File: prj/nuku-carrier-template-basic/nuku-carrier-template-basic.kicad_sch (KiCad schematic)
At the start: 0 parts

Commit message: Route template.basic
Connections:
- no-connect marks 0 -> 2
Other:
- added sheet config (config.kicad_sch)
- added sheet pmod (pmod.kicad_sch)
- sheet bridge ports: added PWREN, SUSPEND, USB_DN, USB_DP, {JTAG}, {UART}; removed none
- sheet core-north-14 ports: added CLK, {CONFIG}; removed none
- sheet usb ports: added USB_DN, USB_DP; removed none

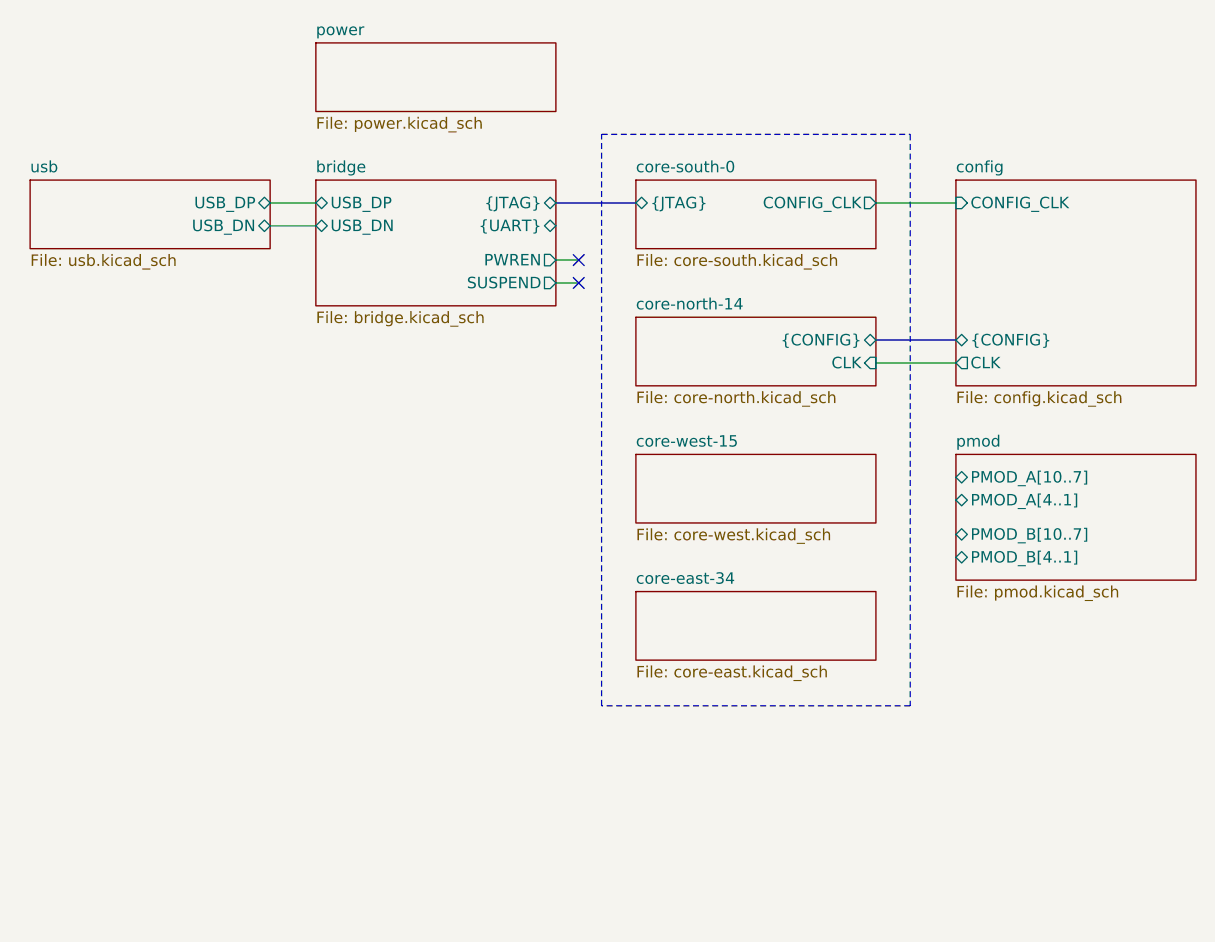
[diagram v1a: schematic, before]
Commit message: Finish template.basic + Production outputs
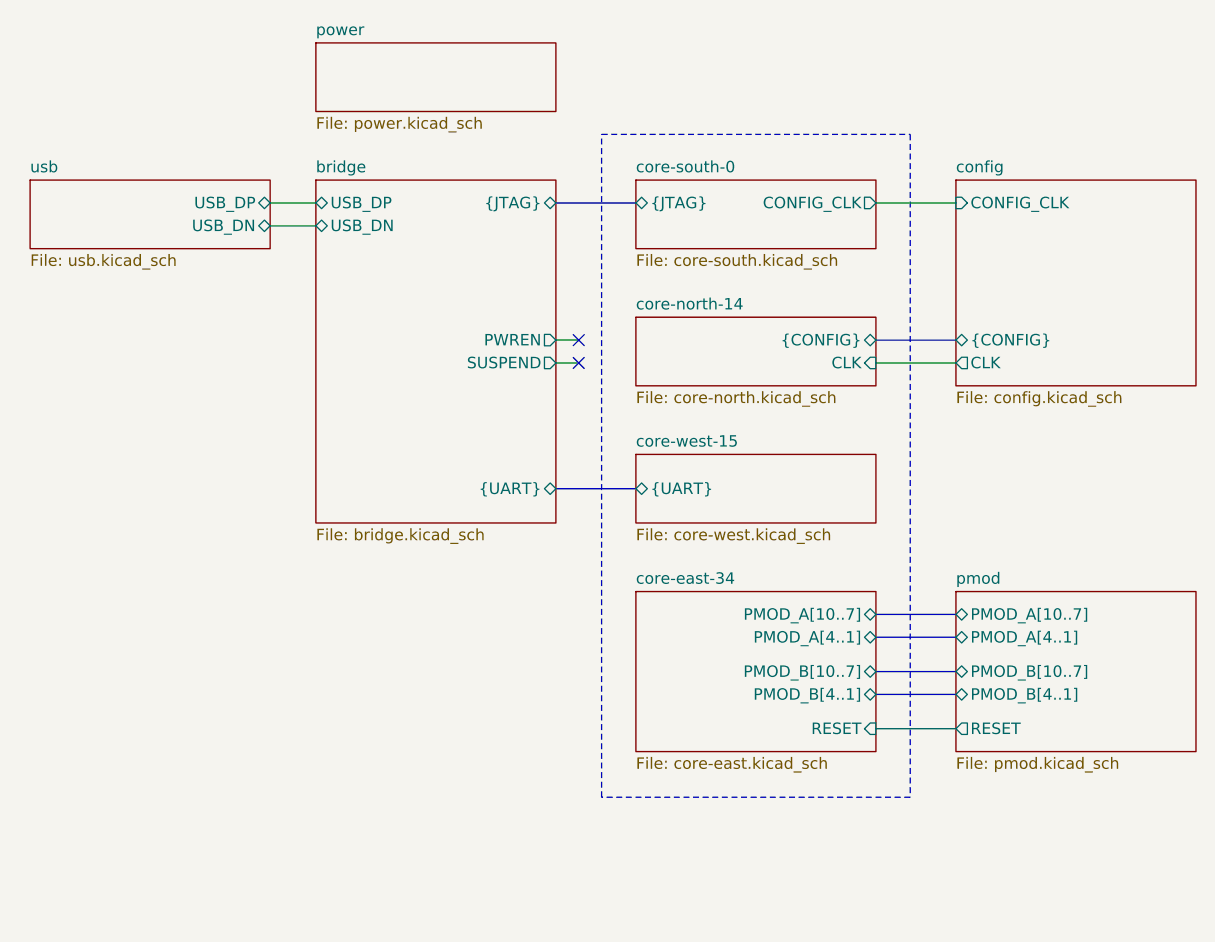
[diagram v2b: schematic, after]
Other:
- sheet core-east-34 ports: added PMOD_A[10..7], PMOD_A[4..1], PMOD_B[10..7], PMOD_B[4..1], RESET; removed none
- sheet core-west-15 ports: added {UART}; removed none
- sheet pmod ports: added RESET; removed none
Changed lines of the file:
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@@
 	(rectangle
 		(start 138.43 66.04)
-		(end 172.72 129.54)
+		(end 172.72 139.7)
 		(stroke
 			(width 0)
@@
 	)
 	(no_connect
-		(at 135.89 80.01)
+		(at 135.89 88.9)
 	)
 	(no_connect
-		(at 135.89 82.55)
+		(at 135.89 91.44)
+	)
+	(bus
+		(pts
+			(xy 168.91 121.92) (xy 177.8 121.92)
+		)
+		(stroke
+			(width 0)
+			(type default)
+		)
+	)
+	(bus
+		(pts
+			(xy 168.91 125.73) (xy 177.8 125.73)
+		)
+		(stroke
+			(width 0)
+			(type default)
+		)
 	)
 	(wire
 		(pts
-			(xy 133.35 80.01) (xy 135.89 80.01)
+			(xy 133.35 88.9) (xy 135.89 88.9)
 		)
 		(stroke
@@
 	(wire
 		(pts
-			(xy 133.35 82.55) (xy 135.89 82.55)
+			(xy 133.35 91.44) (xy 135.89 91.44)
 		)
 		(stroke
@@
 	(bus
 		(pts
+			(xy 168.91 119.38) (xy 177.8 119.38)
+		)
+		(stroke
+			(width 0)
+			(type default)
+		)
+	)
+	(bus
+		(pts
 			(xy 168.91 88.9) (xy 177.8 88.9)
 		)
@@
 	(bus
 		(pts
+			(xy 133.35 105.41) (xy 142.24 105.41)
+		)
+		(stroke
+			(width 0)
+			(type default)
+		)
+	)
+	(bus
+		(pts
 			(xy 133.35 73.66) (xy 142.24 73.66)
 		)
@@
 		)
 	)
+	(bus
+		(pts
+			(xy 168.91 128.27) (xy 177.8 128.27)
+		)
+		(stroke
+			(width 0)
+			(type default)
+		)
+	)
 	(wire
 		(pts
@@
 		(pts
 			(xy 168.91 91.44) (xy 177.8 91.44)
+		)
+		(stroke
+			(width 0)
+			(type default)
+		)
+	)
+	(wire
+		(pts
+			(xy 168.91 132.08) (xy 177.8 132.08)
 		)
 		(stroke
@@
 	(sheet
 		(at 106.68 71.12)
-		(size 26.67 13.97)
+		(size 26.67 38.1)
 		(exclude_from_sim no)
 		(in_bom yes)
@@
 		)
 		(property "Sheetfile" "bridge.kicad_sch"
-			(at 106.68 85.6746 0)
+			(at 106.68 109.8046 0)
 			(effects
 				(font
@@
 		)
 		(pin "PWREN" output
-			(at 133.35 80.01 0)
+			(at 133.35 88.9 0)
 			(effects
 				(font
@@
 		)
 		(pin "SUSPEND" output
-			(at 133.35 82.55 0)
+			(at 133.35 91.44 0)
 			(effects
 				(font
@@
 		)
 		(pin "{UART}" bidirectional
-			(at 133.35 76.2 0)
+			(at 133.35 105.41 0)
 			(effects
 				(font
@@
 	(sheet
 		(at 142.24 116.84)
-		(size 26.67 7.62)
+		(size 26.67 17.78)
 		(exclude_from_sim no)
 		(in_bom yes)
@@
 		)
 		(property "Sheetfile" "core-east.kicad_sch"
-			(at 142.24 125.0446 0)
-			(effects
-				(font
-					(size 1.27 1.27)
-				)
-				(justify left top)
+			(at 142.24 135.2046 0)
+			(effects
+				(font
+					(size 1.27 1.27)
+				)
+				(justify left top)
+			)
+		)
+		(pin "PMOD_A[4..1]" bidirectional
+			(at 168.91 121.92 0)
+			(effects
+				(font
+					(size 1.27 1.27)
+				)
+				(justify right)
+			)
+		)
+		(pin "PMOD_A[10..7]" bidirectional
+			(at 168.91 119.38 0)
+			(effects
+				(font
+					(size 1.27 1.27)
+				)
+				(justify right)
+			)
+		)
+		(pin "PMOD_B[4..1]" bidirectional
+			(at 168.91 128.27 0)
+			(effects
+				(font
+					(size 1.27 1.27)
+				)
+				(justify right)
+			)
+		)
+		(pin "PMOD_B[10..7]" bidirectional
+			(at 168.91 125.73 0)
+			(effects
+				(font
+					(size 1.27 1.27)
+				)
+				(justify right)
+			)
+		)
+		(pin "RESET" input
+			(at 168.91 132.08 0)
+			(effects
+				(font
+					(size 1.27 1.27)
+				)
+				(justify right)
 			)
 		)
@@
 	)
 	(sheet
-		(at 177.8 101.6)
-		(size 26.67 13.97)
+		(at 177.8 116.84)
+		(size 26.67 17.78)
 		(exclude_from_sim no)
 		(in_bom yes)
@@
 		)
 		(property "Sheetname" "pmod"
-			(at 177.8 100.8884 0)
+			(at 177.8 116.1284 0)
 			(effects
 				(font
@@
 		)
 		(property "Sheetfile" "pmod.kicad_sch"
-			(at 177.8 116.1546 0)
+			(at 177.8 135.2046 0)
 			(effects
 				(font
@@
 		)
 		(pin "PMOD_A[4..1]" bidirectional
-			(at 177.8 106.68 180)
+			(at 177.8 121.92 180)
 			(effects
 				(font
@@
 		)
 		(pin "PMOD_A[10..7]" bidirectional
-			(at 177.8 104.14 180)
+			(at 177.8 119.38 180)
 			(effects
 				(font
@@
 		)
 		(pin "PMOD_B[4..1]" bidirectional
-			(at 177.8 113.03 180)
+			(at 177.8 128.27 180)
 			(effects
 				(font
@@
 		)
 		(pin "PMOD_B[10..7]" bidirectional
-			(at 177.8 110.49 180)
+			(at 177.8 125.73 180)
+			(effects
+				(font
+					(size 1.27 1.27)
+				)
+				(justify left)
+			)
+		)
+		(pin "RESET" output
+			(at 177.8 132.08 180)
 			(effects
 				(font
@@
 			)
 		)
+		(pin "{UART}" bidirectional
+			(at 142.24 105.41 180)
+			(effects
+				(font
+					(size 1.27 1.27)
+				)
+				(justify left)
+			)
+		)
